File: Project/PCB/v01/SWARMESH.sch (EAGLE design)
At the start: 50 parts, among them T5 TIP122TIP122, U1 ESP32DEVKITC, U2 TCRT5000L, U3 L293D, U4 L7805CV, U5 TCRT5000L

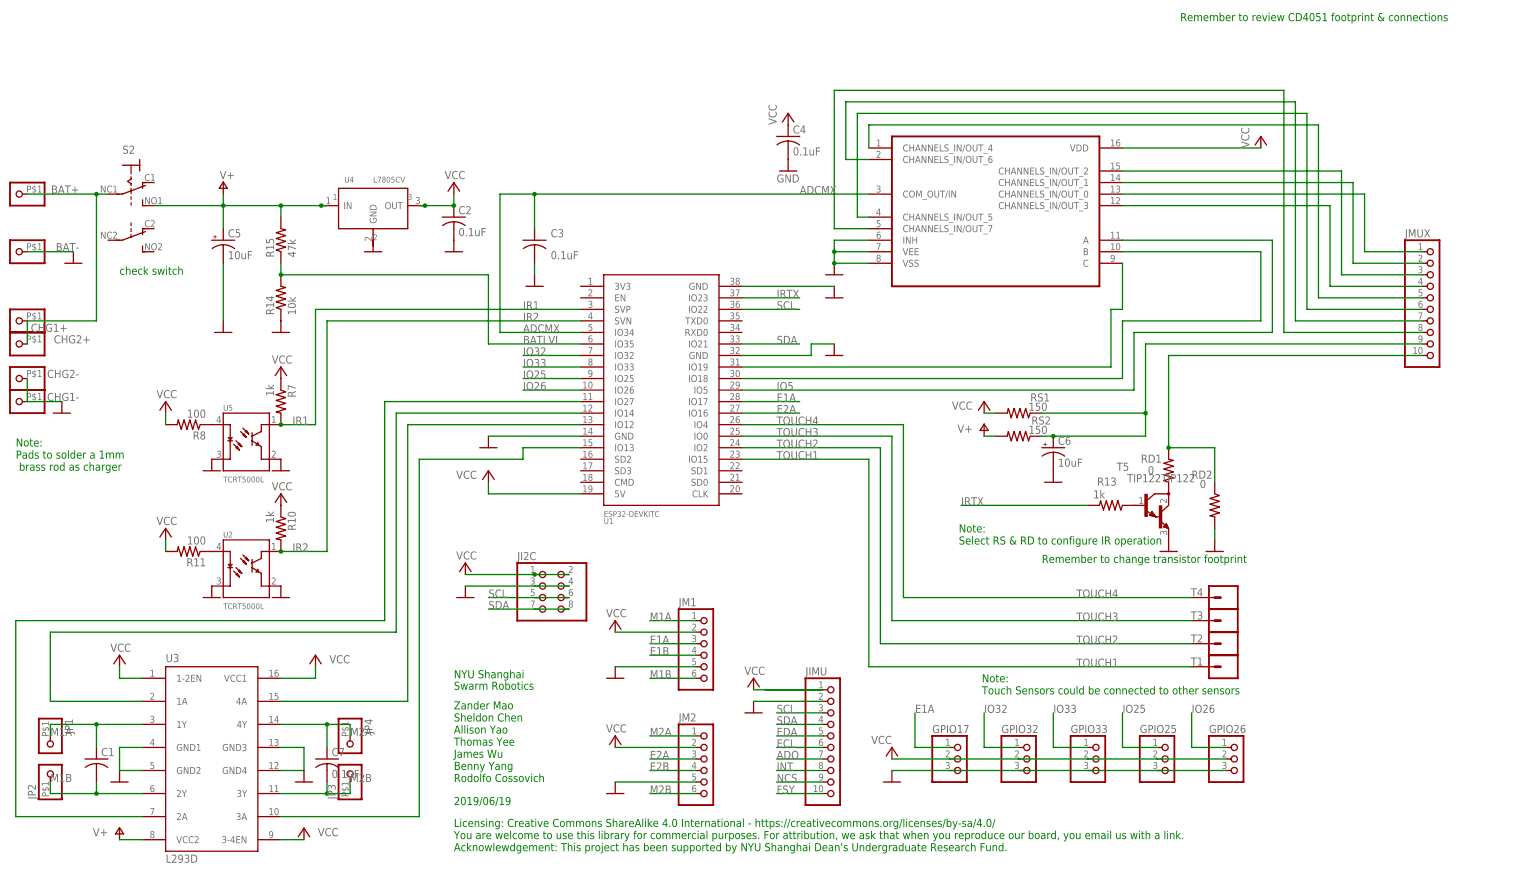
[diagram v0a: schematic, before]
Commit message: update schematic
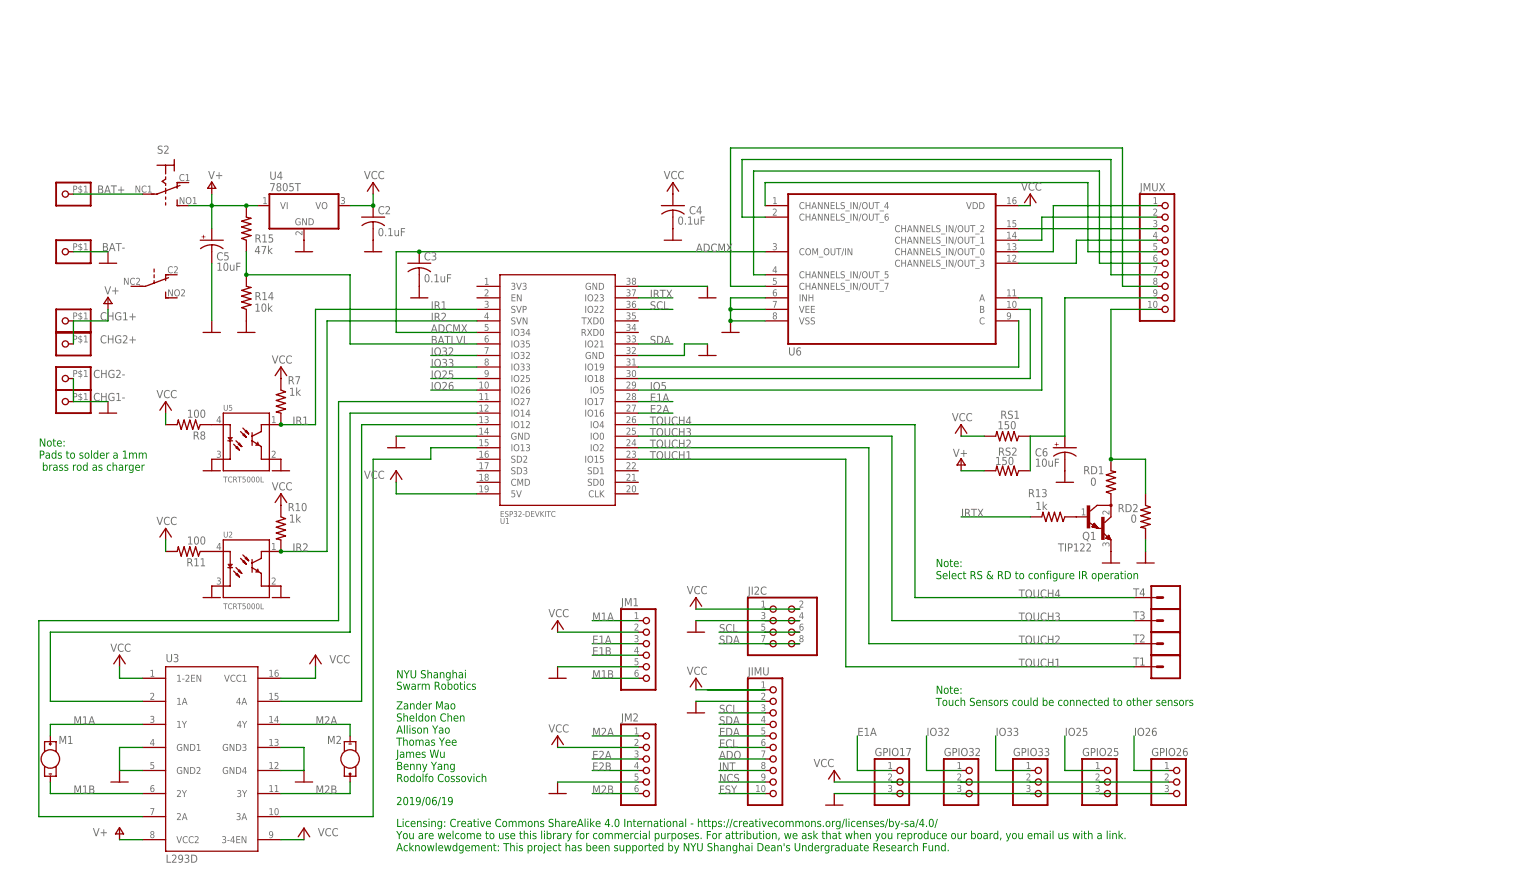
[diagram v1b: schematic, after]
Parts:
- removed C1, C7: 0.1uF, adafruit:C-US050-024X044
- removed JP1, JP2, JP3, JP4: (no value), adafruit:PINHD-1X1-BIGPOGO
- removed T5: TIP122TIP122, TIP122(2):TIP122TIP122
- removed U$1: CD4051BEE4, CD4051BEE4:CD4051BEE4
- added M1, M2: MOTOR10MM, SparkFun-Electromechanical:MOTOR10MM
- added Q1: TIP122, transistor-npn:TIP122
- added U6: CD4051BEE4, CD4051BEE4:CD4051BEE4
- C4: device rcl:C-US025-024X044 -> adafruit:C-US050-024X044
- U4: value L7805CV -> 7805T; device L7805:L7805CV -> adafruit:7805T
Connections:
- removed net N$15 (its old number): BAT+.1, CHG1+.1, CHG2+.1, S21.P
- new net N$21: BAT+.1, S21.P
- new net N$37: Q1.C, RD1.1
- net ADCMX: now also U6.COM_OUT/IN; no longer U$1.COM_OUT/IN
- net GND: now also Q1.E, U4.GND; no longer T5.E, U$1.INH, U$1.VEE, U$1.VSS
- net IO5: now also U6.A; no longer U$1.A
- net M1A: now also M1.+; no longer C1.1, JP1.1
- net M1B: now also M1.-; no longer C1.2, JP2.1
- net M2A: now also M2.-; no longer C7.1, JP4.1
- net M2B: now also M2.+; no longer C7.2, JP3.1
- net N$1: now also Q1.B, R13.1; no longer RD1.1, T5.C
- net N$11: now also JMUX.3, U6.CHANNELS_IN/OUT_2; no longer JMUX.5, U$1.CHANNELS_IN/OUT_4
- net N$12: now also U6.INH, U6.VEE, U6.VSS; no longer R13.1, T5.B
- net N$13: now also U6.CHANNELS_IN/OUT_6; no longer U$1.CHANNELS_IN/OUT_6
- net N$14: now also U6.CHANNELS_IN/OUT_7; no longer U$1.CHANNELS_IN/OUT_7
- net N$2: now also JMUX.5, U6.CHANNELS_IN/OUT_4; no longer JMUX.1, U$1.CHANNELS_IN/OUT_0
- net N$3: now also JMUX.1, U6.CHANNELS_IN/OUT_0; no longer JMUX.2, U$1.CHANNELS_IN/OUT_1
- net N$4: now also JMUX.2, U6.CHANNELS_IN/OUT_1; no longer JMUX.3, U$1.CHANNELS_IN/OUT_2
- net N$5: now also U6.CHANNELS_IN/OUT_5; no longer U$1.CHANNELS_IN/OUT_5
- net N$6: now also U6.CHANNELS_IN/OUT_3; no longer U$1.CHANNELS_IN/OUT_3
- net N$7: now also U6.B; no longer U$1.B
- net N$8: now also U6.C; no longer U$1.C
- net V+: now also CHG1+.1, CHG2+.1, U4.VI; no longer U4.IN
- net VCC: now also U4.VO, U6.VDD; no longer U$1.VDD, U4.OUT
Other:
- note removed: "Remember to change transistor footprint"
- note removed: "Remember to review CD4051 footprint & connections"
- note removed: "check switch"
- moved on the sheet: BAT+, BAT-, C2, C3, C4, C5, C6, CHG1+, CHG1-, CHG2+, CHG2-, GPIO17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
